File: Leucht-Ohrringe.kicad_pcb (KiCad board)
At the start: 2 copper layers, 20 x 49.5 mm, 61 parts, among them J1 Conn_ARM_SWD_TagConnect_TC2030, P1 USB_C_Plug_USB2.0, SW1 SW_SPDT, U1 TX4204, U3 ICM-42670-L, U4 CH340N, U5 nRF52832-QFxx

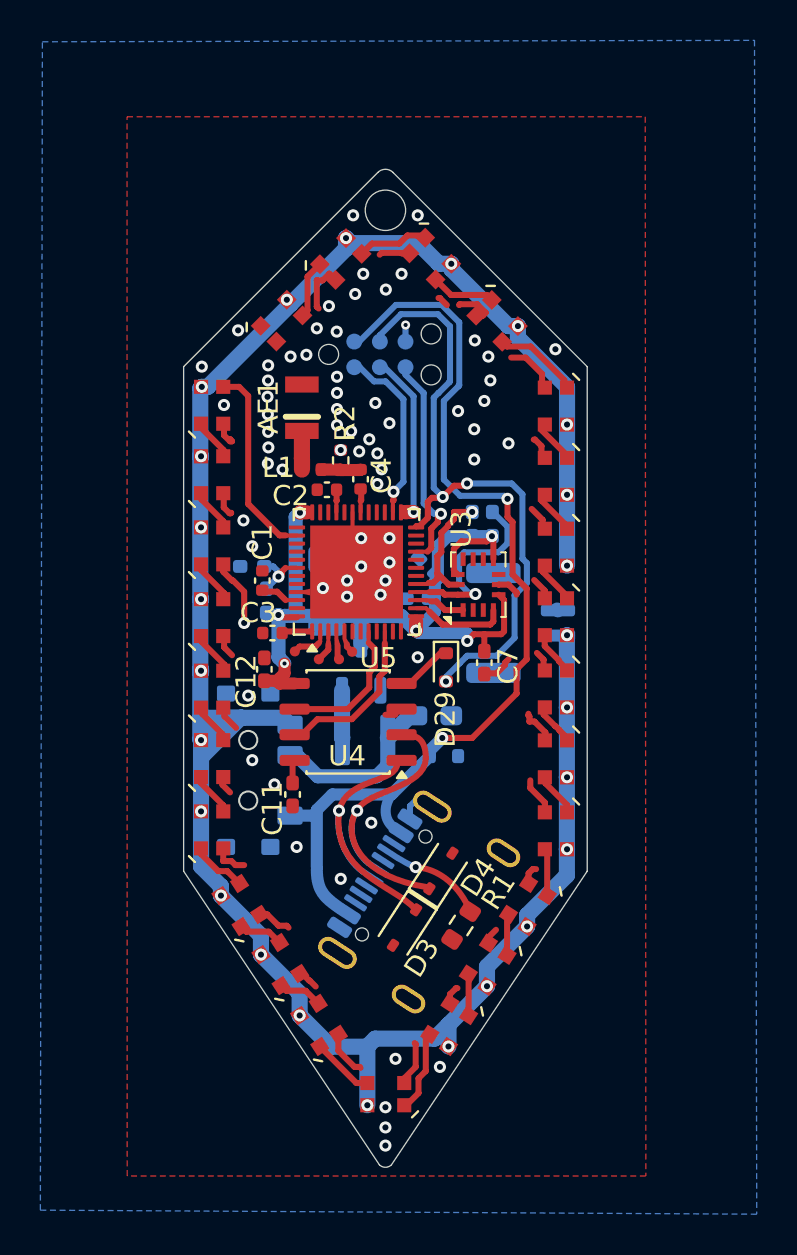
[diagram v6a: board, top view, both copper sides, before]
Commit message: add gpio pads, change to jst sh 1mm
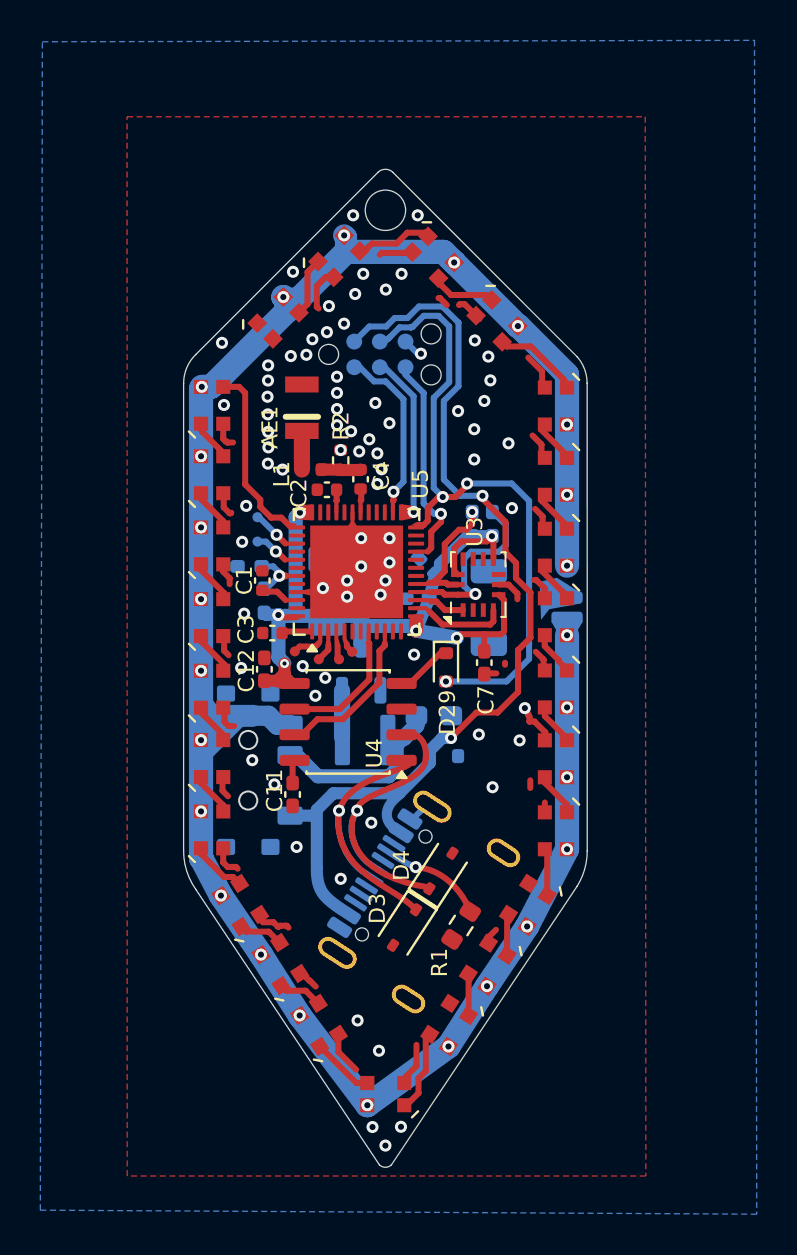
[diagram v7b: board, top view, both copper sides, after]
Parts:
- added TP5: TestPoint, Inductor_SMD:TestPoint_0,5mm, B.Cu at (158.7, 68.7)
- added TP6: TestPoint, Inductor_SMD:TestPoint_0,5mm, B.Cu at (158.7, 67.5)
- BT1: footprint Connector_JST:JST_GH_SM02B-GHS-TB_1x02-1MP_P1.25mm_Horizontal -> Connector_JST:JST_SH_SM02B-SRSS-TB_1x02-1MP_P1.00mm_Horizontal
- moved BT1 0.82 mm to (172.0, 71.9)
- moved D28 0.22 mm to (159.7, 57.6)
- moved D27 0.16 mm to (162.7, 54.5)
- moved D26 0.16 mm to (167.4, 54.6)
- moved TH1 0.13 mm to (158.3, 69.9)
- moved R5 0.11 mm to (159.0, 71.6)
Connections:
- R5 pad 2: Net-(U5-P0.30/AIN6) -> Net-(U5-P0.31/AIN7)
- TH1 pad 1: Net-(U5-P0.30/AIN6) -> Net-(U5-P0.31/AIN7)
- U5 pad 37: unconnected-(U5-P0.25-Pad37) -> LED_IN
- U5 pad 38: LED_IN -> unconnected-(U5-P0.26-Pad38)
- U5 pad 39: unconnected-(U5-P0.27-Pad39) -> Net-(U5-P0.27)
- U5 pad 41: unconnected-(U5-P0.29/AIN5-Pad41) -> Net-(U5-P0.29/AIN5)
- U5 pad 42: Net-(U5-P0.30/AIN6) -> unconnected-(U5-P0.30/AIN6-Pad42)
- U5 pad 43: unconnected-(U5-P0.31/AIN7-Pad43) -> Net-(U5-P0.31/AIN7)
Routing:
- net GND: track 48.6 -> 40.4 mm, vias 69 -> 77
- net Net-(U5-P0.30/AIN6): track 3.20 -> 0.00 mm, vias 1 -> 0
- net VDD: track 41.0 -> 38.4 mm
- net Net-(U5-P0.27): track 0.00 -> 2.50 mm, vias 0 -> 1
- net Net-(U5-P0.29/AIN5): track 0.00 -> 2.33 mm, vias 0 -> 1
- net Net-(U5-P0.31/AIN7): track 0.00 -> 2.04 mm, vias 0 -> 1
- net +BATT: track 111.6 -> 112.9 mm
- net Net-(SW1-B): track 8.63 -> 9.59 mm
- net LED_IN: track 9.81 -> 9.19 mm
- net RESET: track 32.2 -> 32.8 mm
- net Net-(U3-AP_SDA): track 9.95 -> 9.43 mm
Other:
- outline, holes or cut-outs redrawn

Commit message: add ws2812B model, change layout
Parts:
- moved L2 0.87 mm to (163.5, 77.9), turned to 180 degrees
- moved C5 0.22 mm to (166.5, 71.3), turned to -45 degrees
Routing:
- net Net-(SW1-B): track 9.59 -> 8.44 mm
- net GND: track 40.4 -> 40.5 mm, vias 77 -> 80
